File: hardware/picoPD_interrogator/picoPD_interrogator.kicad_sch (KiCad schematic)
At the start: 41 parts, among them Q1 rohm-RE1C002UN, Q2 rohm-RE1C002UN, Q3 rohm-RE1C002UN, Q4 rohm-RE1C002UN, U2 ST-LM393QT, U7 LV2862XDDC

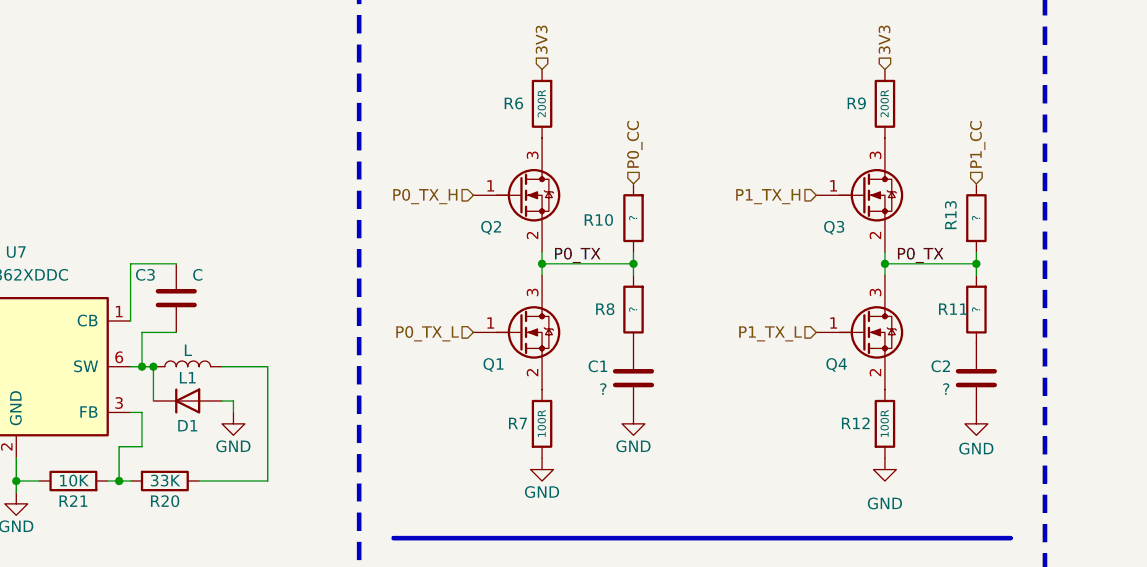
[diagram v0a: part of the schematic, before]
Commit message: Schematic: Added 'Manufacturer PN' field as well as Descriptions to many components.
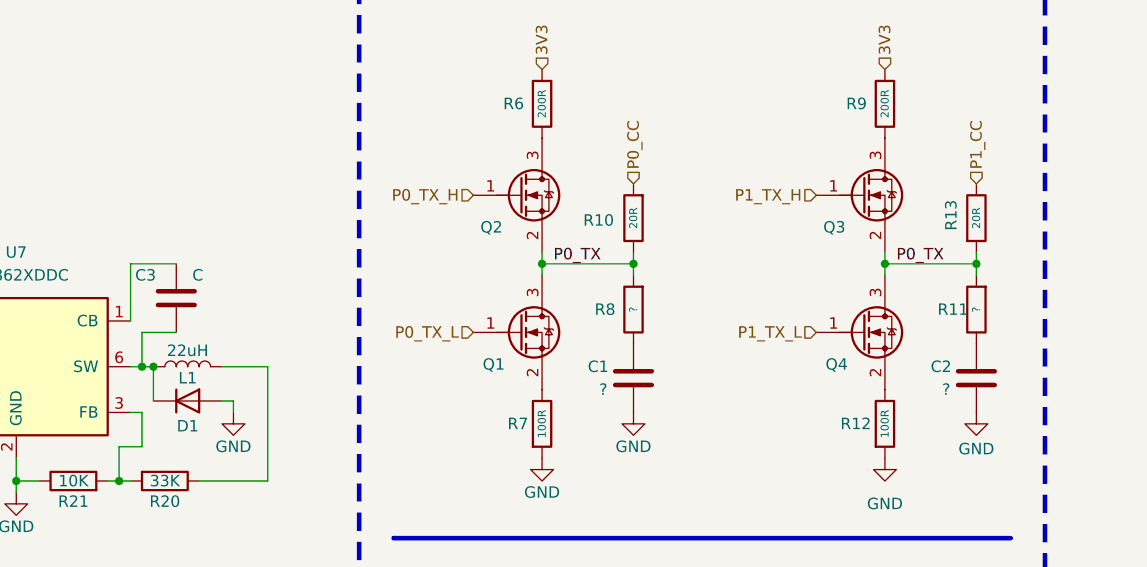
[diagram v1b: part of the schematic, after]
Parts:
- C3: footprint (none) -> Capacitor_SMD:C_0201_0603Metric; Manufacturer PN (none) -> 0201X104K160CT
- D1: footprint (none) -> Diode_SMD:D_SOD-123F; Manufacturer PN (none) -> DSS16U
- J1, J3: footprint picoPD_interrogator:USB-C_GS8 -> picoPD_interrogator:JAE_DX07BN24JA2R1300
- L1: value L -> 22uH; footprint (none) -> Inductor_SMD:L_0805_2012Metric; Manufacturer PN (none) -> MLZ2012P220WT000
- R1: Manufacturer PN (none) -> ERJ-1GNF1001C
- R10, R13: value ? -> 20R; Manufacturer PN (none) -> ERJ-1GNF20R0C
- R12, R7: Manufacturer PN (none) -> ERJ-1GNF1000C
- R14, R15: Manufacturer PN (none) -> ERJ-1GNF5101C
- R16, R17: Manufacturer PN (none) -> ERJ-1GNF4701C
- R18, R19: Manufacturer PN (none) -> ERJ-1GNF33R0C
- R2, R4, R5: Manufacturer PN (none) -> ERJ-1GNF3301C
- R20: footprint (none) -> Resistor_SMD:R_0201_0603Metric; Manufacturer PN (none) -> ERJ-1GNF3302C
- R21: footprint (none) -> Resistor_SMD:R_0201_0603Metric; Manufacturer PN (none) -> ERJ-1GNF1002C
- R22: footprint (none) -> Resistor_SMD:R_0201_0603Metric; Manufacturer PN (none) -> ERJ-1GNF1003C
- R6, R9: Manufacturer PN (none) -> ERJ-1GNF2000C
- U3, U4: footprint (none) -> picoPD_interrogator:NXP_NX3DV3899GU; Manufacturer PN (none) -> NX3DV3899GU,115
- U5, U6: footprint (none) -> picoPD_interrogator:TI_sn741vc1g3157-q1; Manufacturer PN (none) -> 1P1G3157QDCKRQ1

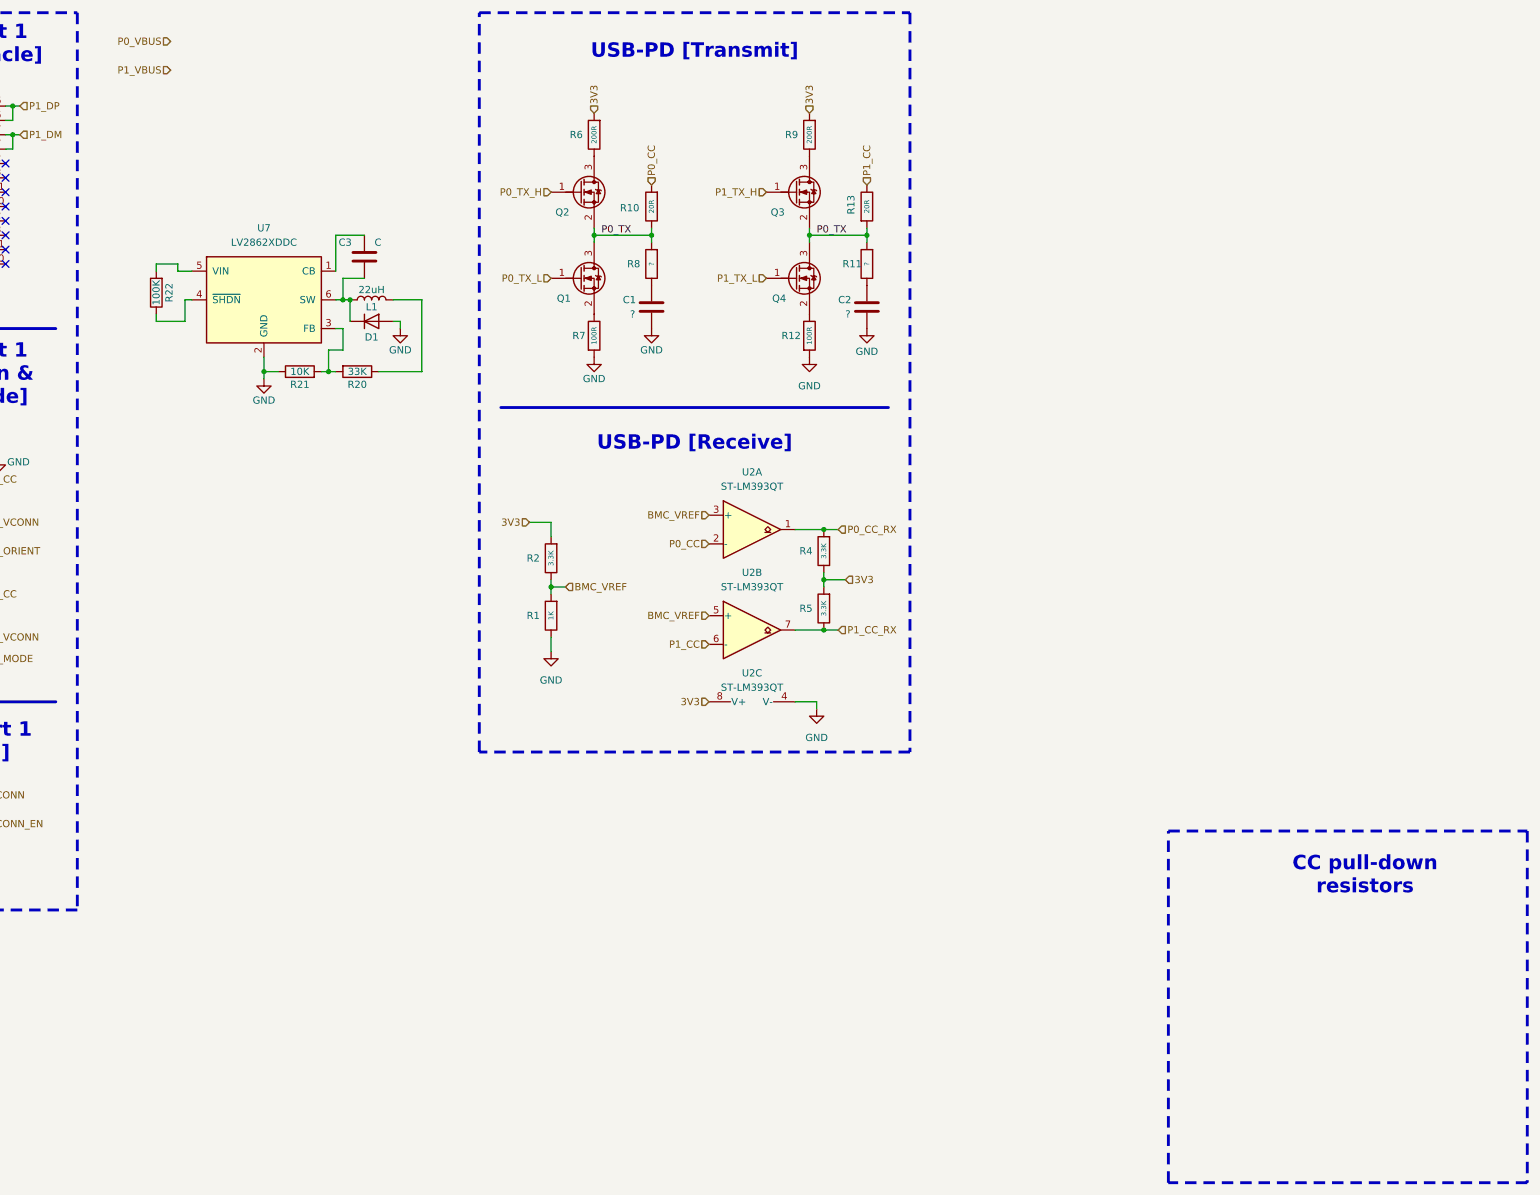
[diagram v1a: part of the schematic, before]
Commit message: Schematic: Added 3.3v buck converter circuit.
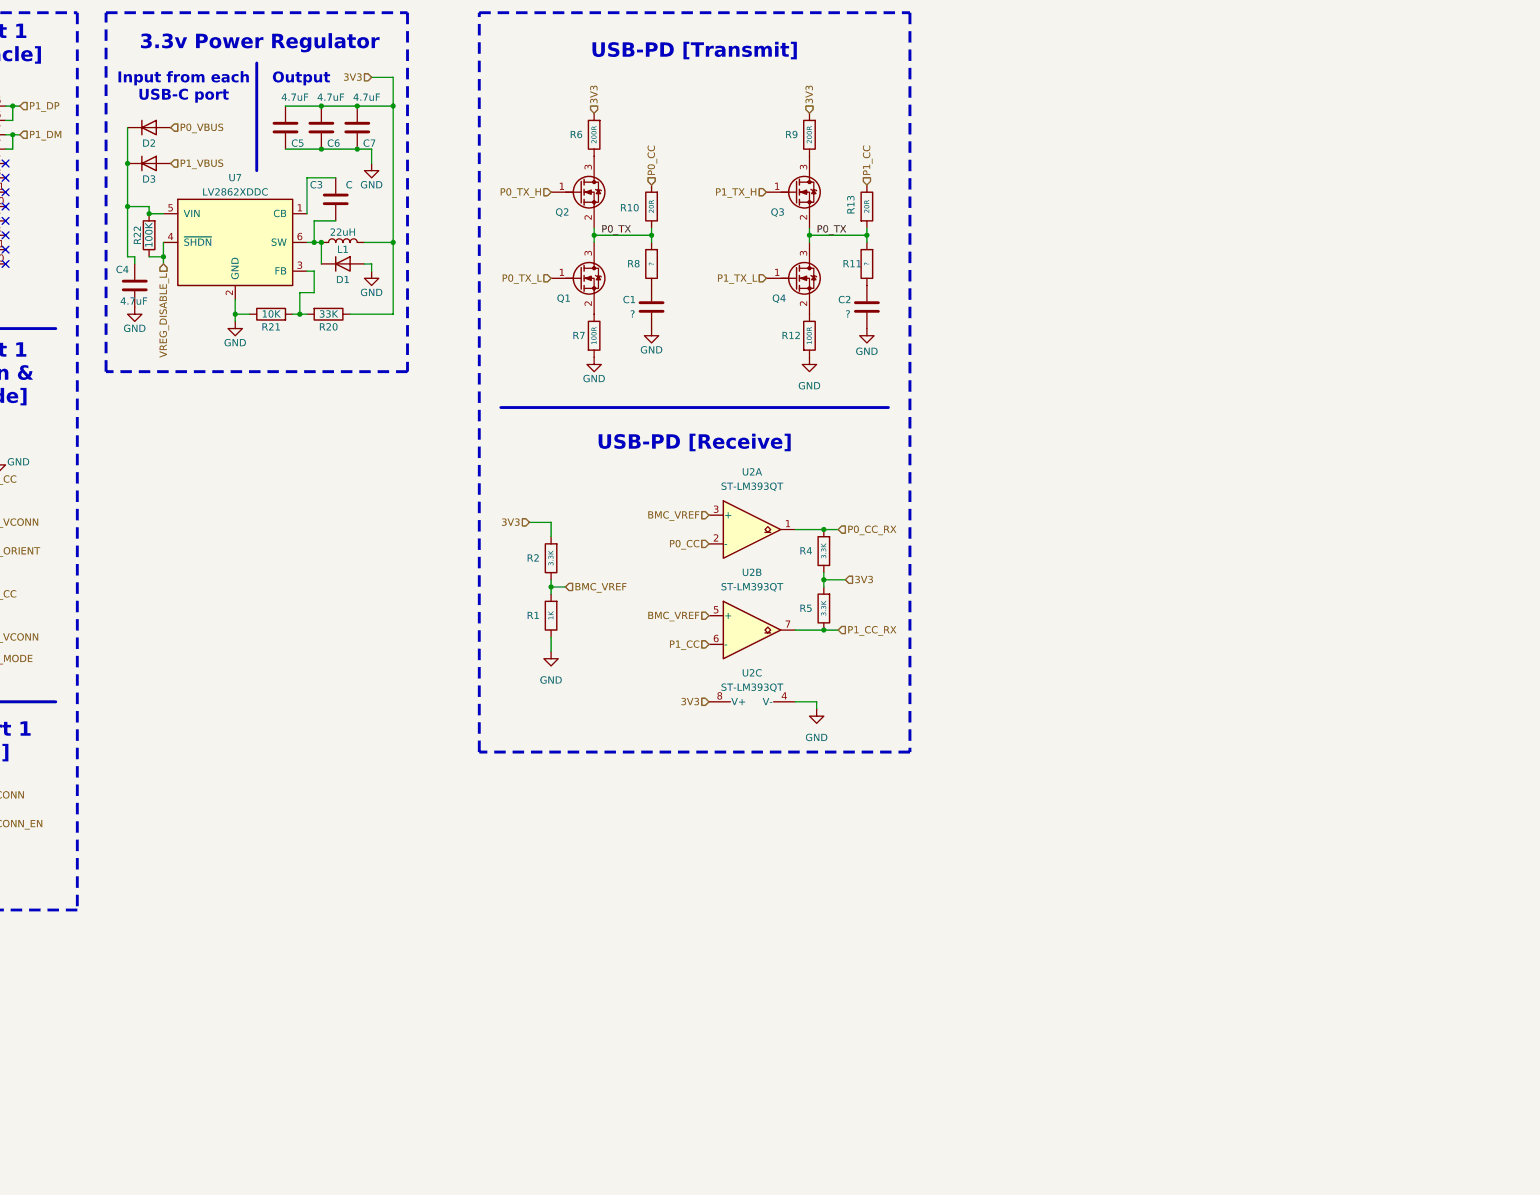
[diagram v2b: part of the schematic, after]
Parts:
- added C4, C5, C6, C7: 4.7uF, Capacitor_SMD:C_0603_1608Metric, symbol Device:C
- added D2, D3: D, Diode_SMD:D_SOD-123F, symbol Device:D
- U2: Description 2 (none) -> IC COMPARATOR 2 GEN PUR 8UFSON; Manufacturer PN (none) -> LM393QT
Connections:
- net 3V3: now also L1.2, R20.1, C5.1, C6.1, C7.1
- net GND: now also C4.1, C5.2, C6.2, C7.2
- net P0_VBUS: now also D2.2 (A)
- net P1_VBUS: now also D3.2 (A)
- net VREG_DISABLE_L: now reaches R22.1, U7.4 (~{SHDN})
- net at R22.2, U7.5 (VIN): now also C4.2, D2.1 (K), D3.1 (K)
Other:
- note added: "3.3v Power Regulator"
- note added: "Input from each USB-C port"
- note added: "Output"
- note removed: "CC pull-down resistors"
- moved on the sheet: C3, D1, L1, R20, R21, R22, U7

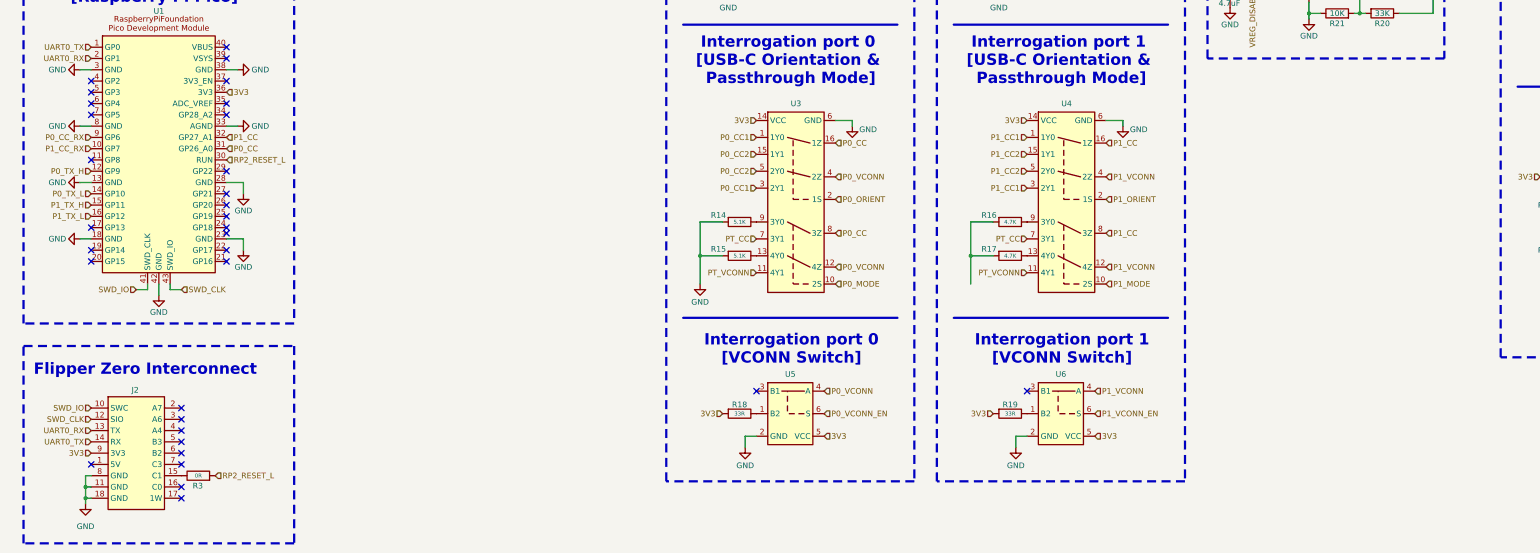
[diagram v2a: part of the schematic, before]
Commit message: Schematic: Shut down 3V3 reg while flipper is attached.
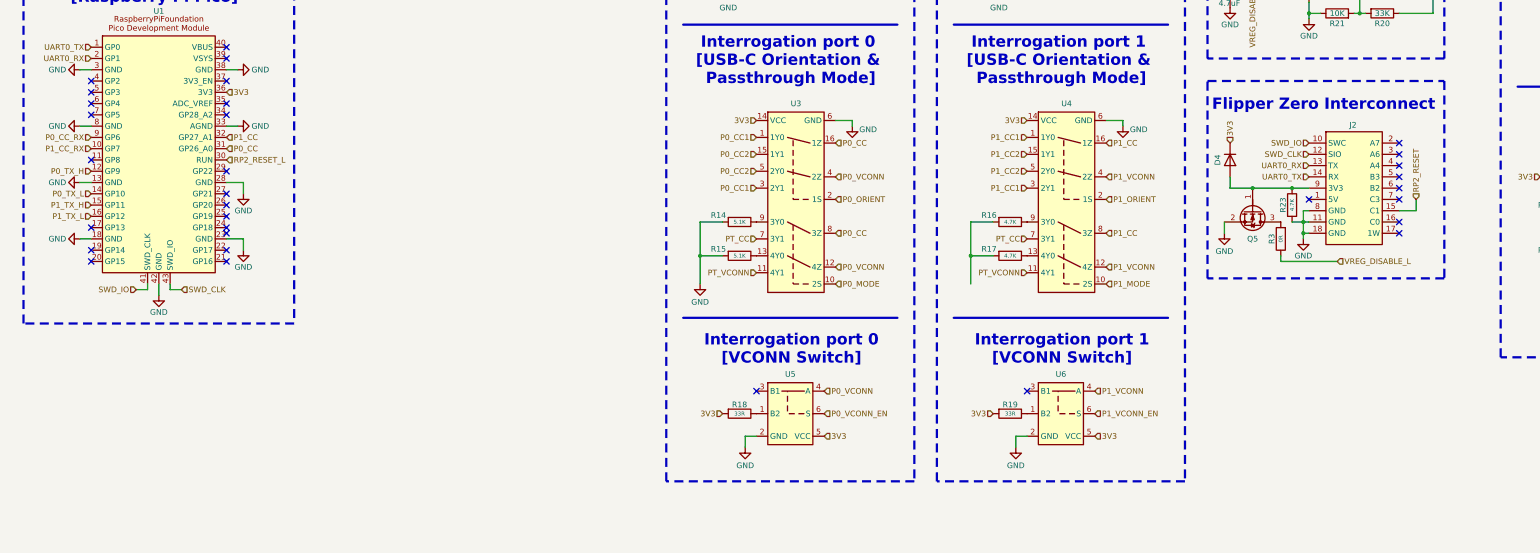
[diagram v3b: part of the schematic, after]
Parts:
- added D4: D, Diode_SMD:D_SOD-123F, symbol Device:D
- added Q5: rohm-RE1C002UN, Package_TO_SOT_SMD:SOT-416, symbol picoPD_interrogator:rohm-RE1C002UN
- added R23: 4.7K, Resistor_SMD:R_0201_0603Metric, symbol Device:R
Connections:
- net 3V3: now also D4.1 (K); no longer J2.9 (3V3)
- net GND: now also Q5.2 (S), R23.2
- net RP2_RESET_L: no longer R3.2
- net VREG_DISABLE_L: now also R3.1
- net RP2_RESET: now reaches J2.15 (C1)
- net RP2_RESET: no longer R3.1
- new net: D4.2 (A), J2.9 (3V3), Q5.1 (G), R23.1
- new net: Q5.3 (D), R3.2
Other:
- moved on the sheet: J2, R3
